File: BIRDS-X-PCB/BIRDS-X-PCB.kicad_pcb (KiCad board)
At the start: 4 copper layers, 85 x 85 mm, 87 parts, among them J101 LPC-50M2LG, J102 Conn_02x04_Odd_Even, J201 Conn_01x02, J202 Conn_01x02, J203 Conn_01x02, J401 Conn_01x04, J402 Conn_01x08, J403 Conn_01x02, J404 MHDR2X5, Q201 SI1470DH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

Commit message: Add logos and final labels
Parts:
- added G***: LOGO, BIRDS-X_Footprints_Lib:AlbertaSat_Logo_25x20mm, B.Cu at (108.8, 107.2)
- added G***: LOGO, BIRDS-X_Footprints_Lib:CTS_Logo_50x25mm, B.Cu at (109.0, 89.6)
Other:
- board text added: "AlbertaSat x CalgaryToSpace 2023-04-28"
- board text added: "Git: xxx"
- board text added: "JASPER BIRDS-X Rev1"

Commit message: Final changes for rev1
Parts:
- Q201, Q202: value SI1470DH -> AO3420; footprint Package_TO_SOT_SMD:SOT-363_SC-70-6 -> Package_TO_SOT_SMD:SOT-23
- R205: value 1k -> 10k
- SW401: footprint Button_Switch_SMD:SW_Push_SPST_NO_Alps_SKRK -> Button_Switch_SMD:SW_Tactile_SPST_NO_Straight_CK_PTS636Sx25SMTRLFS
- U203: value 0.1S7B_3UP -> 0.1S7B_0512S3UP
- moved SW401 3.45 mm to (70.9, 70.0)
- moved Q201 2.07 mm to (89.3, 96.6)
- moved Q202 1.52 mm to (76.9, 96.3)
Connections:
- Q201 pad 1: /PowerSheet/5V_Current_Sense -> Net-(Q201-G)
- Q201 pad 2: /PowerSheet/5V_Current_Sense -> +5V
- Q201 pad 3: Net-(Q201-G) -> /PowerSheet/5V_Current_Sense
- Q202 pad 1: /PowerSheet/3V3_Current_Sense -> Net-(Q202-G)
- Q202 pad 2: /PowerSheet/3V3_Current_Sense -> +3V3
- Q202 pad 3: Net-(Q202-G) -> /PowerSheet/3V3_Current_Sense
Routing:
- net GND: track 47.6 -> 34.1 mm, vias 43 -> 49
- net /PowerSheet/3V3_Current_Sense: track 19.3 -> 11.7 mm
- net /PowerSheet/5V_Current_Sense: track 17.7 -> 12.1 mm
- net Net-(Q201-G): track 9.11 -> 11.0 mm, vias 2 -> 0
- net Net-(JP403-B): track 23.2 -> 25.1 mm
- net ST_SWDIO: track 82.6 -> 80.9 mm
- net DIO2_5V_EN_FROM_BOSS: track 37.4 -> 35.7 mm, vias 2 -> 1
- net Net-(Q202-G): track 9.74 -> 8.30 mm, vias 2 -> 0
- net Net-(J402-Pin_7): track 50.6 -> 49.3 mm
- net Net-(J403-Pin_1): track 29.6 -> 28.7 mm
- net Net-(U303-DIODE_ANODE): track 77.3 -> 78.1 mm
- net +12V: track 103.7 -> 104.3 mm
- net ST_RST: track 90.5 -> 89.9 mm, vias 6 -> 7
- net Net-(R302-Pad1): track 24.0 -> 24.6 mm
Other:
- board text added: "Reset"

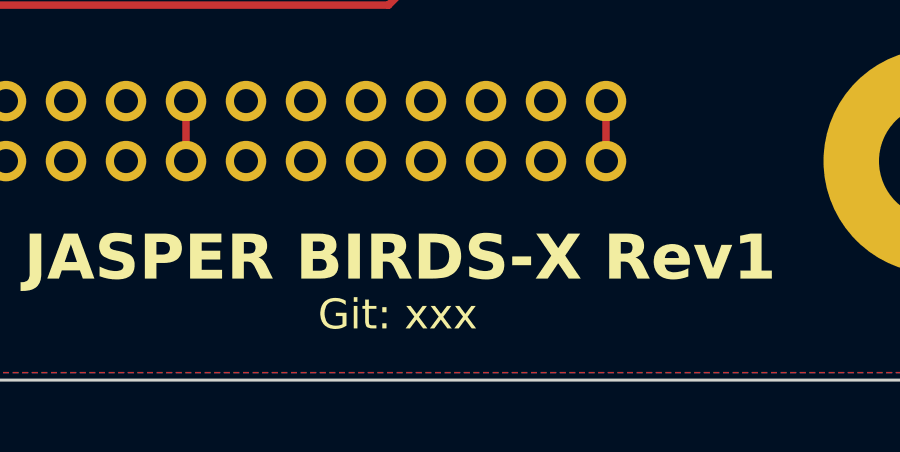
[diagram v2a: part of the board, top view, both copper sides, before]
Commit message: Add teardrops
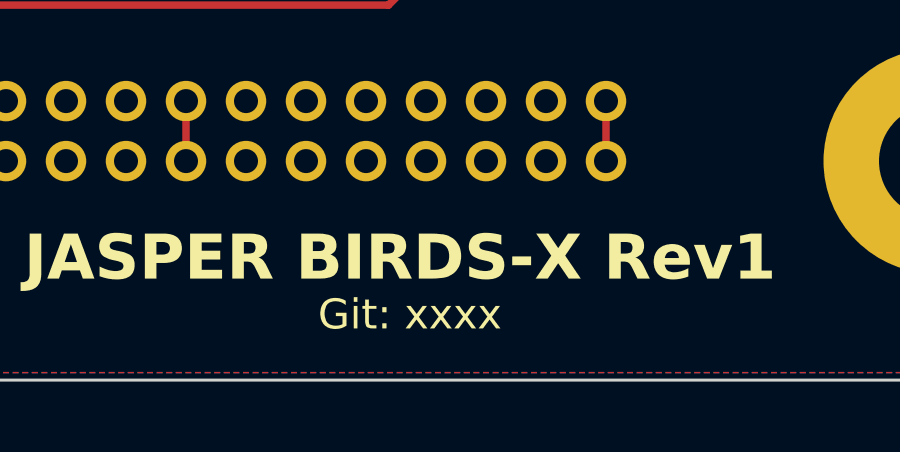
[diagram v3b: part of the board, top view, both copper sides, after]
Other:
- board text added: "Git: xxxx"
- board text removed: "Git: xxx"

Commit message: Export gerbers
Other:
- board text added: "Git: 7fbbad6"
- board text removed: "Git: xxxx"

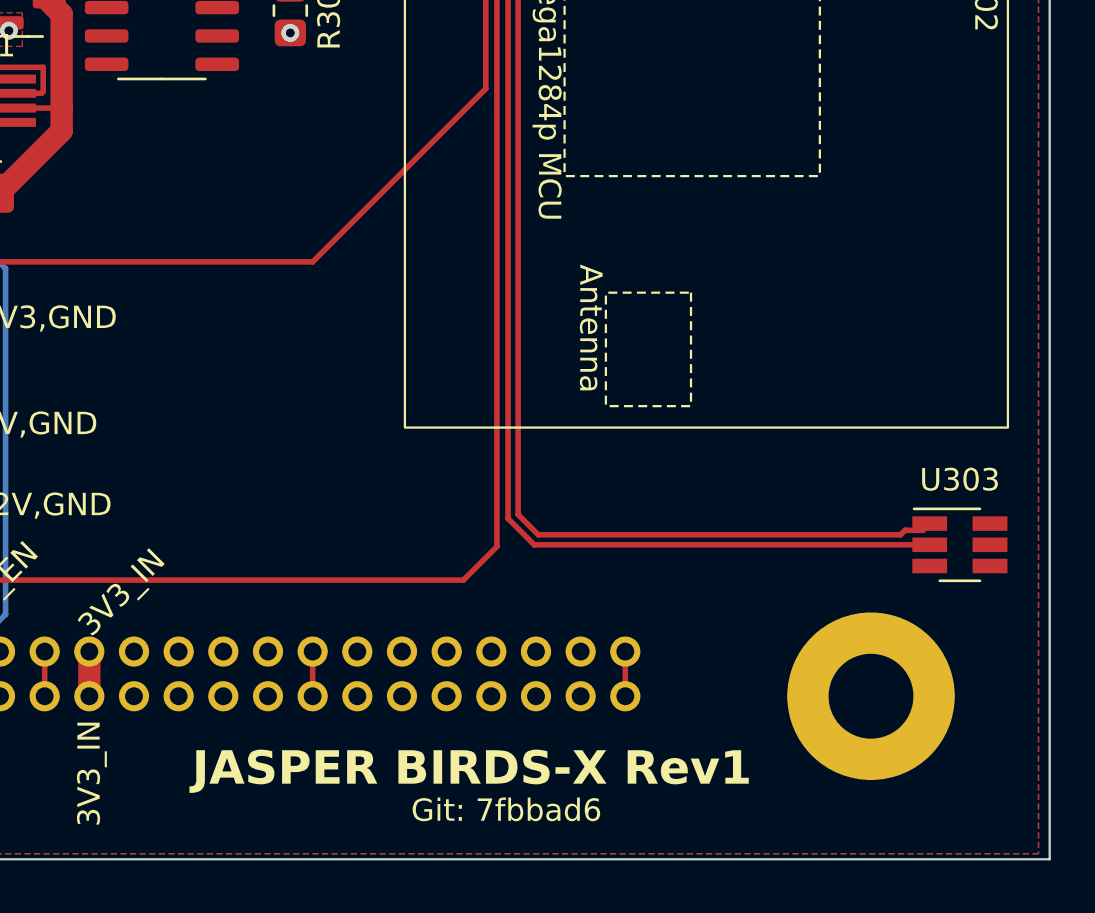
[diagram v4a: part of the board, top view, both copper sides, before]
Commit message: Add text silk screen areas
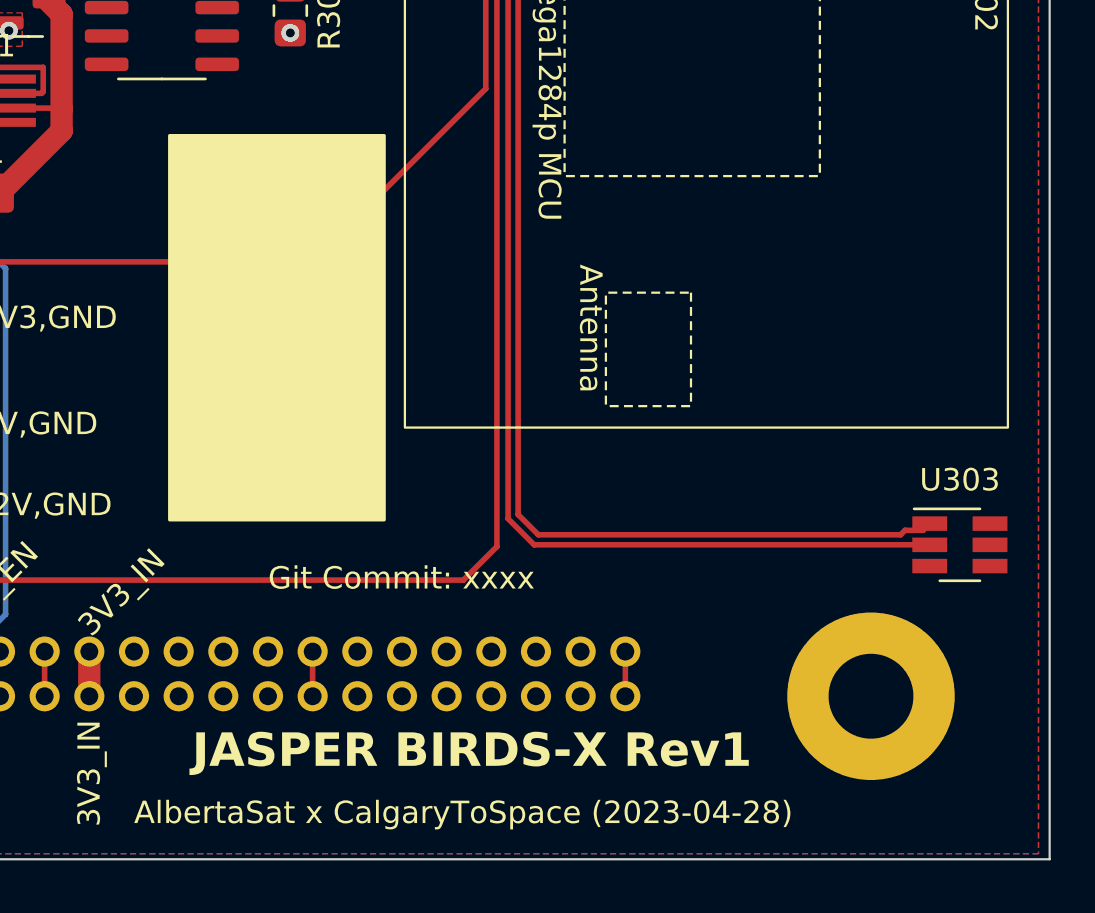
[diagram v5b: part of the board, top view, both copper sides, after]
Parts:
- moved G*** 1.25 mm to (107.9, 89.0)
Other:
- board text added: "AlbertaSat x CalgaryToSpace (2023-04-28)"
- board text added: "Git Commit: xxxx"
- board text removed: "Git: 7fbbad6"
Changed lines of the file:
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@@
   )
   (footprint "BIRDS-X_Footprints_Lib:CTS_Logo_50x25mm" (layer "B.Cu")
-    (at 109 89.6 180)
+    (at 107.904074 89 180)
     (attr board_only exclude_from_pos_files exclude_from_bom)
     (fp_text reference "G***" (at -0.2 -6.4) (layer "B.SilkS") hide
@@
     )
   )
+  (gr_rect (start 65.5 57) (end 118.5 77)
+    (stroke (width 0.15) (type solid)) (fill solid) (layer "B.SilkS"))
+  (gr_rect (start 62 57) (end 80 121)
+    (stroke (width 0.15) (type solid)) (fill solid) (layer "B.SilkS"))
+  (gr_rect (start 95.6 102.6) (end 105.2 119.8)
+    (stroke (width 0.15) (type solid)) (fill solid) (layer "F.SilkS"))
   (gr_line locked (start 135 135) (end 50 135)
     (stroke (width 0.1) (type default)) (layer "Edge.Cuts"))
@@
     (effects (font (size 1 1) (thickness 0.15)) (justify right))
   )
-  (gr_text "JASPER BIRDS-X Rev1" (at 96.6 131.8) (layer "F.SilkS")
+  (gr_text "JASPER BIRDS-X Rev1" (at 96.6 131) (layer "F.SilkS")
     (effects (font (size 1.5 1.5) (thickness 0.3) bold) (justify left bottom))
   )
@@
     (effects (font (size 1 1) (thickness 0.15)) (justify right))
   )
-  (gr_text "Git: 7fbbad6" (at 106.4 133.4) (layer "F.SilkS")
+  (gr_text "AlbertaSat x CalgaryToSpace (2023-04-28)" (at 94 133.5) (layer "F.SilkS")
     (effects (font (size 1 1) (thickness 0.15)) (justify left bottom))
   )
@@
     (effects (font (size 1 1) (thickness 0.15)) (justify left))
   )
+  (gr_text "Git Commit: xxxx" (at 100 123) (layer "F.SilkS")
+    (effects (font (size 1 1) (thickness 0.15)) (justify left bottom))
+  )
   (gr_text "GND" (at 55 100) (layer "F.SilkS")
